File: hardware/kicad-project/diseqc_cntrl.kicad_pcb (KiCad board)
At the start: 4 copper layers, 90 x 100 mm, 124 parts, among them IC1 TPS560200DBVR, IC2 STM32F407VGT6, IC3 USBLC6-2P6, IC4 FM24CL16B-GTR, IC5 LNBH26PQR, IC6 W5500, J1 Barrel Jack, J2 Conn_01x04_Pin, J3 Conn_01x04_Pin, J4 USB4110-GF-A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

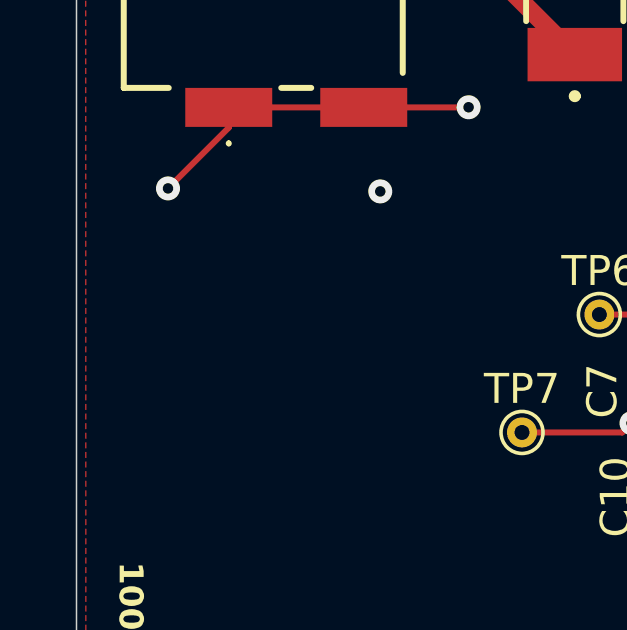
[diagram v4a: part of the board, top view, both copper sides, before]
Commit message: Added ground pad for easier testing
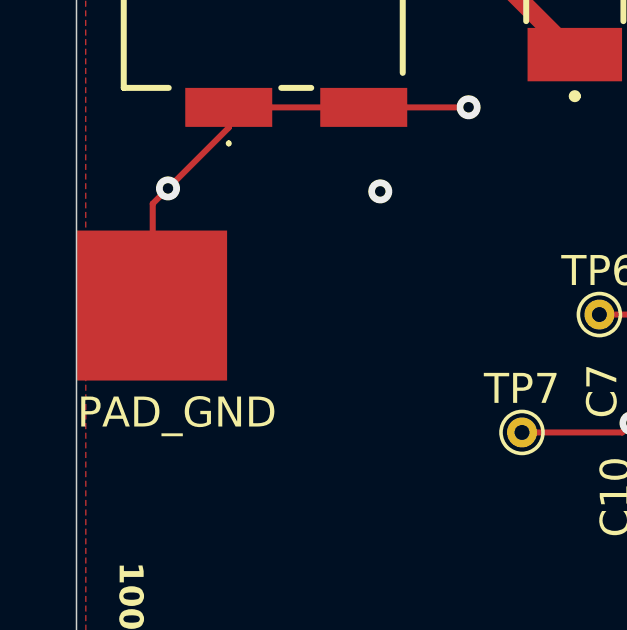
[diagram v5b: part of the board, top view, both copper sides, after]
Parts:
- added PAD_GND: GND, private:Ground Pad 5mm, left edge, F.Cu at (50.0, 83.9)
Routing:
- net GND: track 225.9 -> 230.0 mm
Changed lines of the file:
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@@
 		(embedded_fonts no)
 	)
+	(footprint "private:Ground Pad 5mm, left edge"
+		(layer "F.Cu")
+		(at 50.02 83.88)
+		(property "Reference" "PAD_GND"
+			(at 3.33 6.07 0)
+			(unlocked yes)
+			(layer "F.SilkS")
+			(effects
+				(font
+					(size 1 1)
+					(thickness 0.125)
+				)
+			)
+		)
+		(property "Value" "GND"
+			(at 1.5 7.5 0)
+			(unlocked yes)
+			(layer "F.Fab")
+			(effects
+				(font
+					(size 1 1)
+					(thickness 0.15)
+				)
+			)
+		)
+		(property "Datasheet" ""
+			(at 0 0 0)
+			(unlocked yes)
+			(layer "F.Fab")
+			(hide yes)
+			(effects
+				(font
+					(size 1 1)
+					(thickness 0.15)
+				)
+			)
+		)
+		(property "Description" ""
+			(at 0 0 0)
+			(unlocked yes)
+			(layer "F.Fab")
+			(hide yes)
+			(effects
+				(font
+					(size 1 1)
+					(thickness 0.15)
+				)
+			)
+		)
+		(attr smd)
+		(fp_text user "${REFERENCE}"
+			(at 5.5 -1 0)
+			(unlocked yes)
+			(layer "F.Fab")
+			(effects
+				(font
+					(size 1 1)
+					(thickness 0.15)
+				)
+			)
+		)
+		(pad "1" smd rect
+			(at 2.5 2.5)
+			(size 5 5)
+			(property pad_prop_testpoint)
+			(layers "F.Cu" "F.Mask" "F.Paste")
+			(net 1 "GND")
+		)
+		(embedded_fonts no)
+	)
 	(footprint "Resistor_SMD:R_0603_1608Metric_Pad0.98x0.95mm_HandSolder"
 		(layer "F.Cu")
@@
 	)
 	(segment
+		(start 52.54 86.38)
+		(end 52.54 82.985)
+		(width 0.2)
+		(layer "F.Cu")
+		(net 1)
+	)
+	(segment
 		(start 86.8 109.2)
 		(end 88.55 110.95)
@@
 		(width 0.2)
 		(layer "F.Cu")
+		(net 1)
+	)
+	(segment
+		(start 52.54 82.985)
+		(end 53.05 82.475)
+		(width 0.2)
+		(layer "F.Cu")

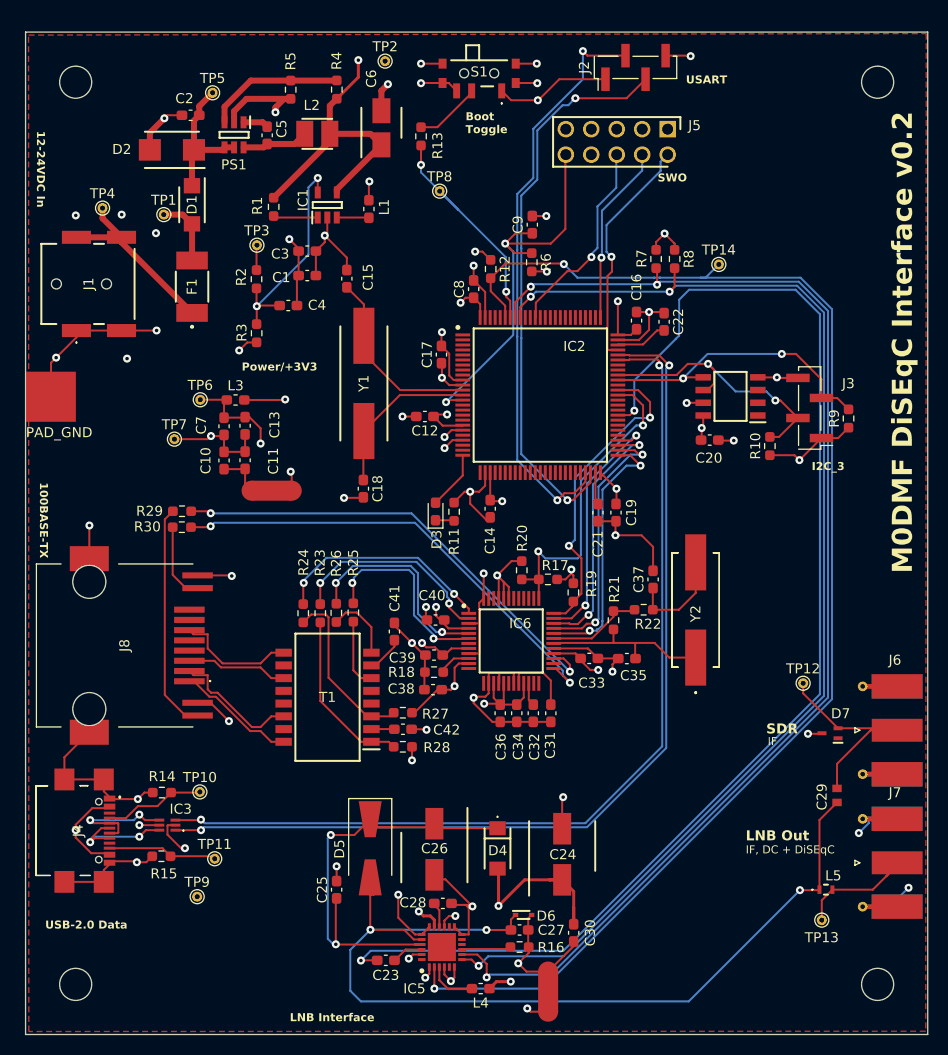
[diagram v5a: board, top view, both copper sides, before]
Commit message: Moved SWD to TC2050 connector
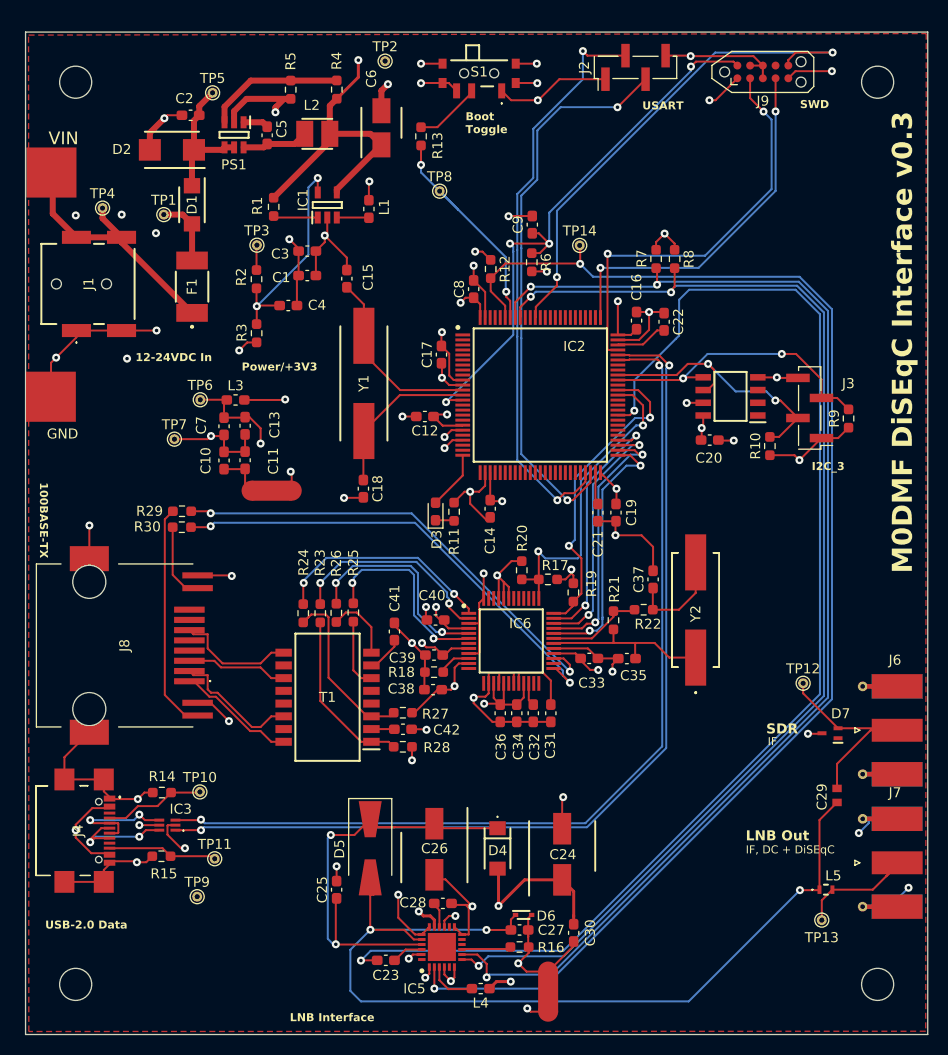
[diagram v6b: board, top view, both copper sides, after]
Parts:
- removed J5: SWD, diseqc_cntrl:HDRV10W64P254_2X5_1270X495X838P
- added J9: Conn_ARM_SWD_TagConnect_TC2030, Connector:Tag-Connect_TC2050-IDC-NL_2x05_P1.27mm_Vertical, F.Cu at (123.5, 54.0)
- added VIN: , , F.Cu at (52.6, 64.0)
- moved TP14 14.0 mm to (105.3, 71.3)
- renumbered PAD_GND to GND
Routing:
- net /MCU/SWO: track 20.2 -> 50.9 mm, vias 1 -> 2
- net +3V3: track 132.6 -> 153.1 mm, vias 25 -> 26
- net /MCU/SWCLK: track 18.0 -> 36.8 mm, vias 1 -> 2
- net /MCU/SWDIO: track 23.4 -> 41.8 mm, vias 1 -> 2
- net /MCU/NRST: track 40.9 -> 57.2 mm, vias 2 -> 4
- net GND: track 230.0 -> 246.0 mm, vias 44 -> 45
- net VIN_RAW: track 18.7 -> 26.2 mm
- net +12V: track 204.2 -> 202.2 mm
- net Net-(D4-K): track 47.1 -> 45.3 mm
- net PGND: track 40.3 -> 42.1 mm
- net TD-: track 17.2 -> 18.1 mm
- net /MCU/LNBH26PQR/LNB_FLT: track 136.1 -> 135.6 mm
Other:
- board text added: "M0DMF DiSEqC Interface v0.3"
- board text added: "SWD"
- board text removed: "M0DMF DiSEqC Interface v0.2"
- board text removed: "SWO"

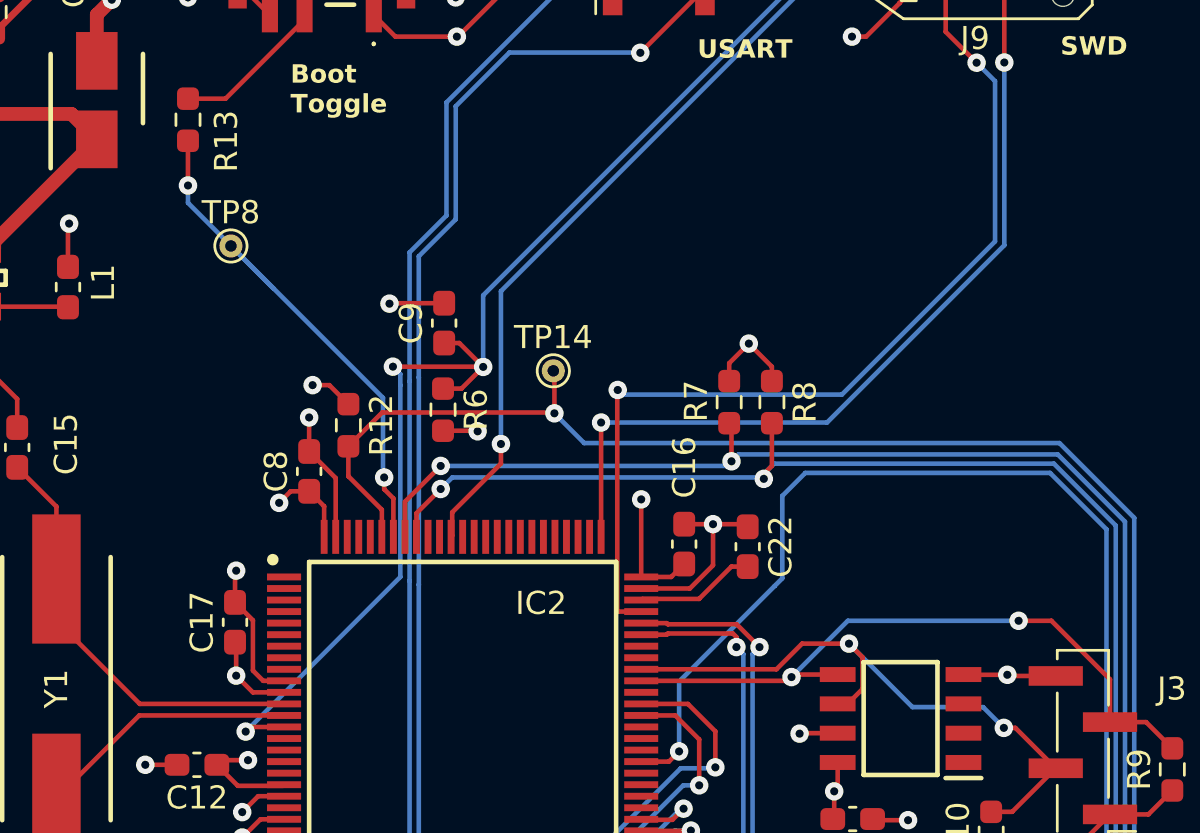
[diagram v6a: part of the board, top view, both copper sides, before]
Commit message: Fix: VBAT should be connected to VDD
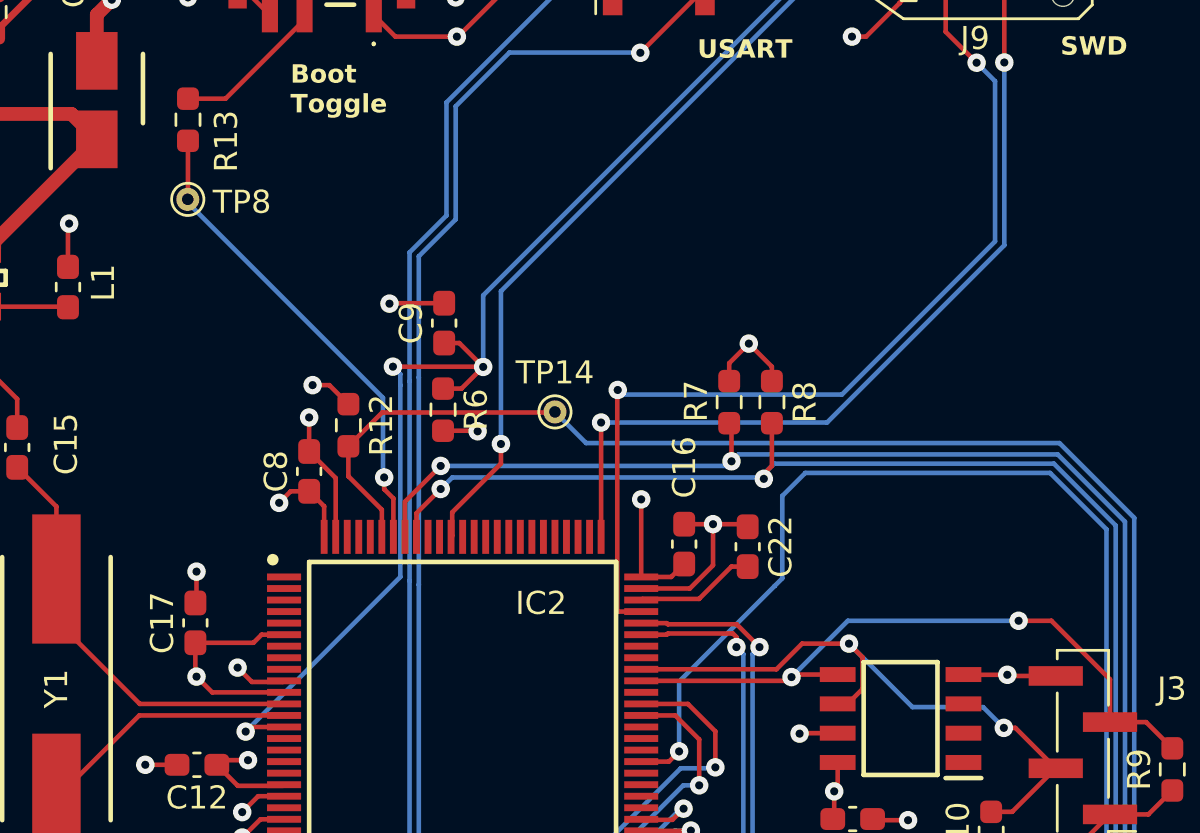
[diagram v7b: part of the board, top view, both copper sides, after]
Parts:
- moved TP8 2.75 mm to (89.4, 63.9)
- moved TP14 1.78 mm to (105.3, 73.1)
- moved C17 1.72 mm to (89.8, 82.2)
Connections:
- IC2 pad 6: unconnected-(IC2-VBAT-Pad6) -> +3V3
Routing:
- net +3V3: track 153.1 -> 158.9 mm
- net /MCU/BOOT0: track 23.4 -> 20.9 mm, vias 2 -> 1
- net GND: track 246.0 -> 243.6 mm, vias 45 -> 46
- net /MCU/LNBH26PQR/LNB_FLT: track 135.6 -> 133.8 mm, vias 2 -> 1

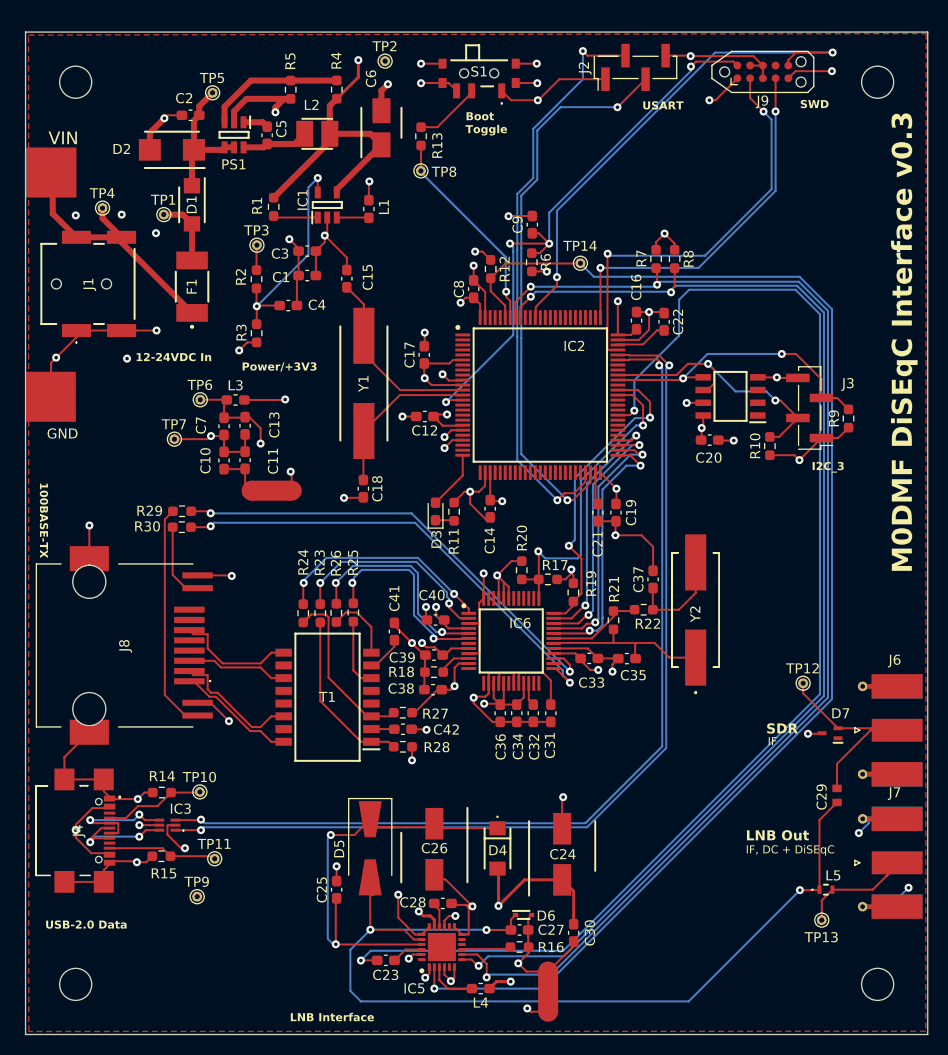
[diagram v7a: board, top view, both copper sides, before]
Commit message: Fix: Add VBUS sense to MCU for USB DFU
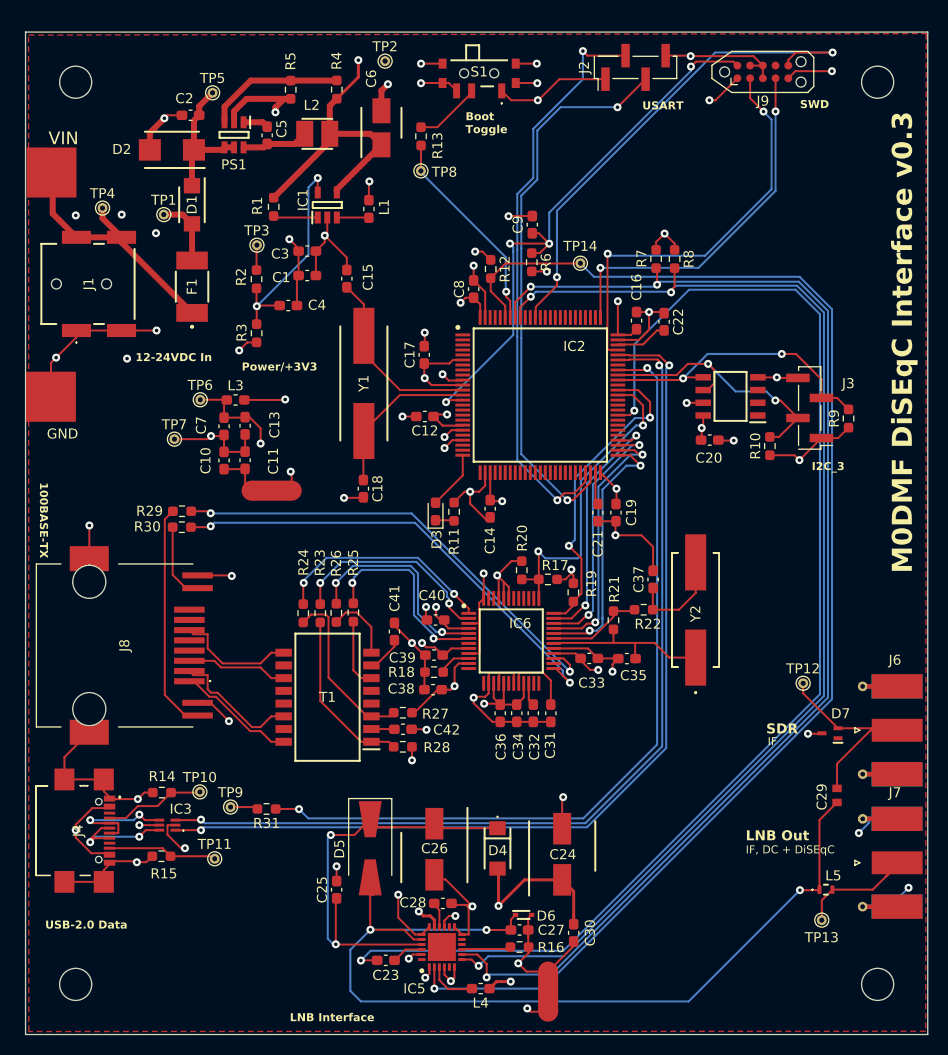
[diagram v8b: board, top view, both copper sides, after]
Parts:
- added R31: 100k, Resistor_SMD:R_0603_1608Metric_Pad0.98x0.95mm_HandSolder, F.Cu at (74.0, 127.5)
- moved TP9 9.54 mm to (70.5, 127.3)
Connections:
- IC2 pad 68: unconnected-(IC2-PA9-Pad68) -> /MCU/VBUS_SENSE
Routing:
- net /MCU/VBUS_SENSE: track 0.00 -> 82.5 mm, vias 0 -> 2
- net VBUS: track 34.3 -> 31.2 mm
